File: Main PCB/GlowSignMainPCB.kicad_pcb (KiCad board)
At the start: 2 copper layers, 169.5 x 83.5 mm, 159 parts, among them P1 Thermal_Pad, P2 Thermal_Pad, P3 Thermal_Pad, P4 Thermal_Pad, P5 Thermal_Pad, P6 Thermal_Pad, SW1 TS-1185EC-C-D-B, SW2 TS-1185EC-C-D-B, SW3 TS24CA, U1 S8050, U10 TP4056, U11 DW01A, U12 AO3400A, U13 AP40P05, U14 AP40P05, U15 SS54, U16 AP40P05, U17 SS54, U18 BL1117-33CX, U2 SS54, U20 MSM261D4030H1CPM, U26 M1250RS-02P, U3 SN74LVC2T45DCUR, U4 ESP32-WROOM-32E, U5 FP6276BXR-G1, U6 SS54, U7 CP2102-GMR, U8 UMH3N, U9 FS8205A

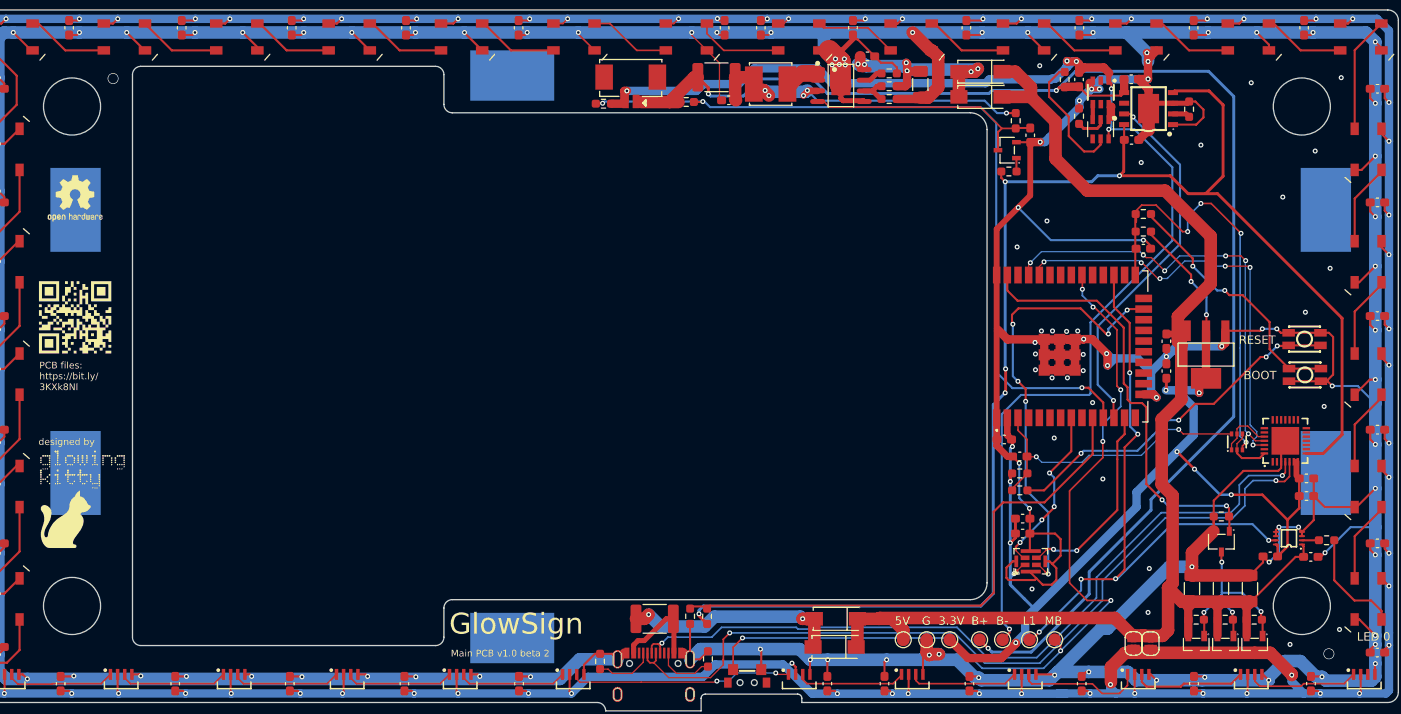
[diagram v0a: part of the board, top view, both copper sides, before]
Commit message: fixed important mistake... VBUS not connected...
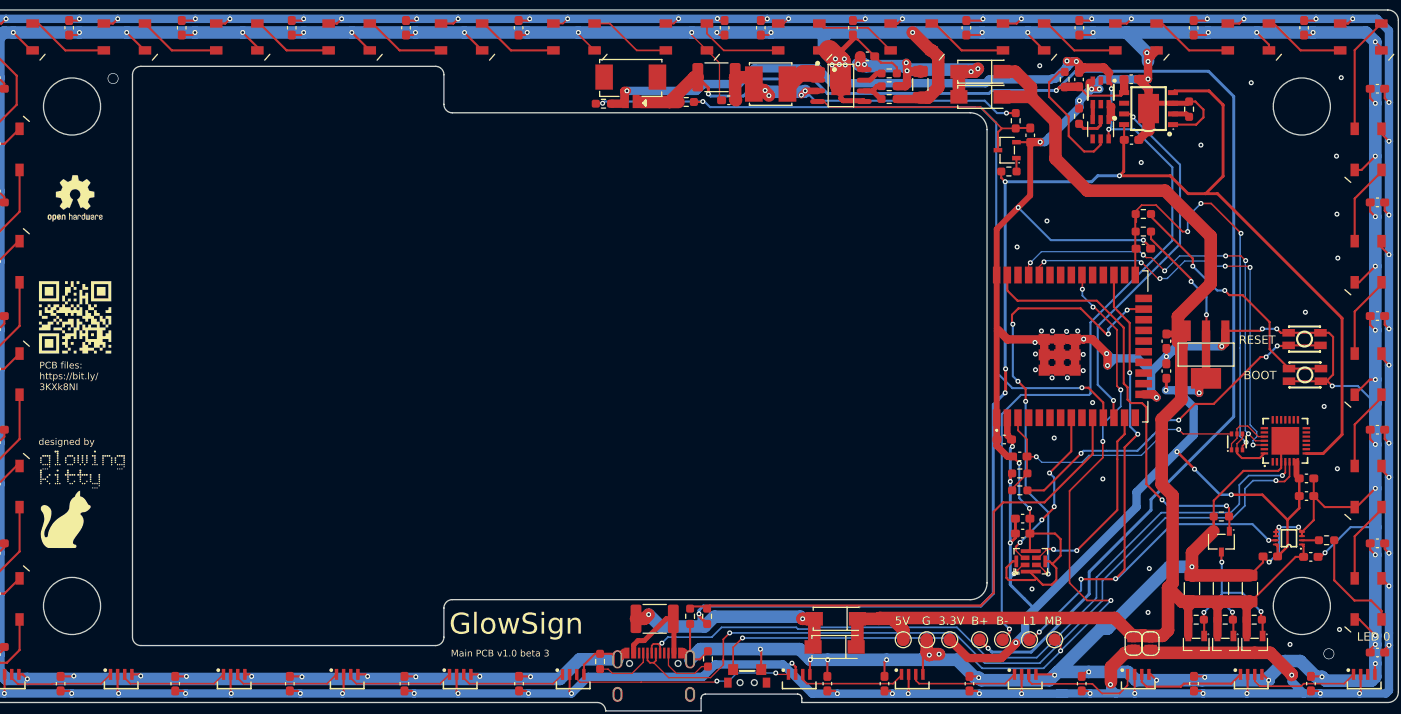
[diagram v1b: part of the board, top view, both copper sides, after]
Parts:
- removed P1, P2, P3, P4, P5, P6: Thermal_Pad, footprint:Thermal pad
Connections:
- F1 pad 2: Net-(F1-Pad2) -> VBUS
- U17 pad 2: Net-(F1-Pad2) -> VBUS
- U2 pad 2: Net-(F1-Pad2) -> VBUS
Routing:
- net VBUS: track 180.0 -> 207.9 mm, vias 5 -> 7
- net Net-(F1-Pad2): track 26.1 -> 0.00 mm, vias 2 -> 0
- net GND: track 1002.7 -> 1002.9 mm, vias 129 -> 130
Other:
- board text added: "Main PCB v1.0 beta 3"
- board text removed: "Main PCB v1.0 beta 2"
